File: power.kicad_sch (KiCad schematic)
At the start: 84 parts, among them J5 VJ1, Q1 BC857, Q2 2N7002, U1 LFE5U-85F-6BG381C, U3 TLV62569DBV, U4 TLV62569DBV, U5 TLV62569DBV, U7 MCP7940NT, Y2 32768Hz

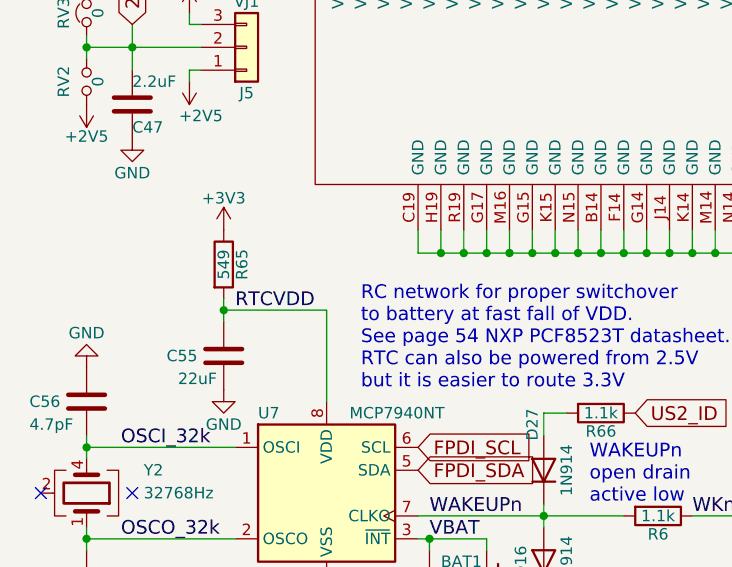
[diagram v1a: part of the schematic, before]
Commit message: add PWR_PIN to RTCVDD
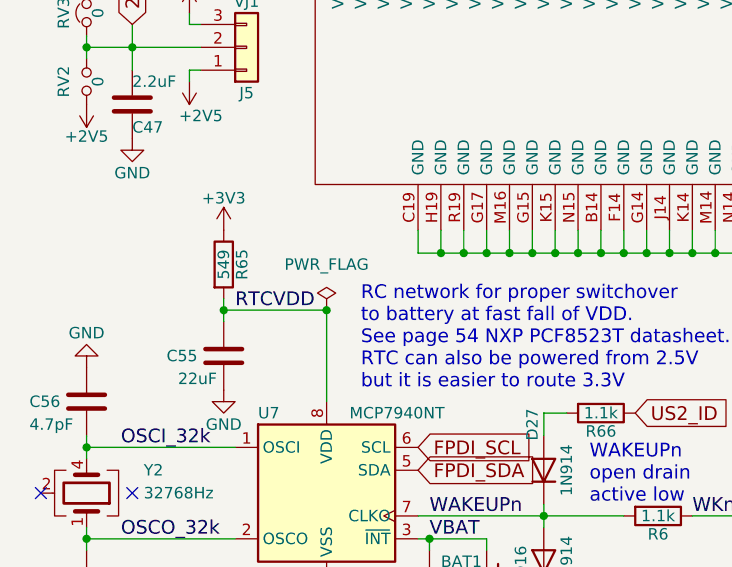
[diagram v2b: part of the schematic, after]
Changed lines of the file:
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@@
 	)
 	(junction
+		(at 49.53 72.39)
+		(diameter 0)
+		(color 0 0 0 0)
+	)
+	(junction
 		(at 247.65 66.04)
 		(diameter 0)
@@
 					(unit 1)
 				)
+			)
+		)
+	)
+	(symbol
+		(lib_id "power:PWR_FLAG")
+		(at 49.53 72.39 0)
+		(unit 1)
+		(exclude_from_sim no)
+		(in_bom yes)
+		(on_board yes)
+		(dnp no)
+		(fields_autoplaced yes)
+		(property "Reference" "#FLG02"
+			(at 49.53 70.485 0)
+			(effects
+				(font
+					(size 1.27 1.27)
+				)
+				(hide yes)
+			)
+		)
+		(property "Value" "PWR_FLAG"
+			(at 49.53 67.31 0)
+			(effects
+				(font
+					(size 1.27 1.27)
+				)
+			)
+		)
+		(property "Footprint" ""
+			(at 49.53 72.39 0)
+			(effects
+				(font
+					(size 1.27 1.27)
+				)
+				(hide yes)
+			)
+		)
+		(property "Datasheet" "~"
+			(at 49.53 72.39 0)
+			(effects
+				(font
+					(size 1.27 1.27)
+				)
+				(hide yes)
+			)
+		)
+		(property "Description" "Special symbol for telling ERC where power comes from"
+			(at 49.53 72.39 0)
+			(effects
+				(font
+					(size 1.27 1.27)
+				)
+				(hide yes)
+			)
+		)
+		(pin "1"
+		)
+		(instances
+			(project "ulx3s"
+				(path "/49a43414-f3c1-43b2-ad20-ac3166075f21/00000000-0000-0000-0000-000058d51cad"
+					(reference "#FLG02")
+					(unit 1)
+				)

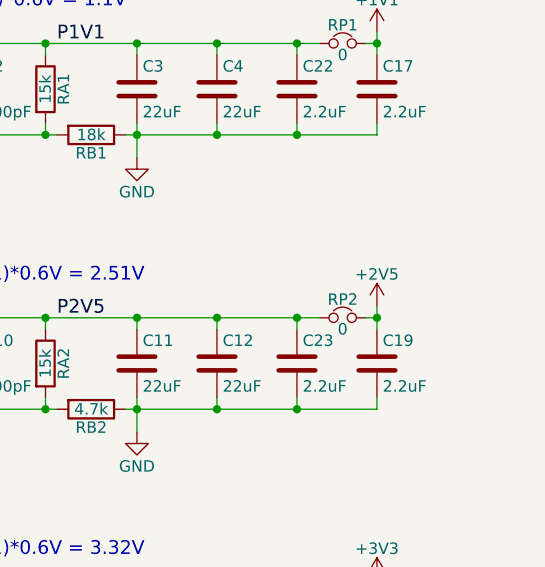
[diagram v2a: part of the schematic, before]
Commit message: add pwr_pin to 2.5v
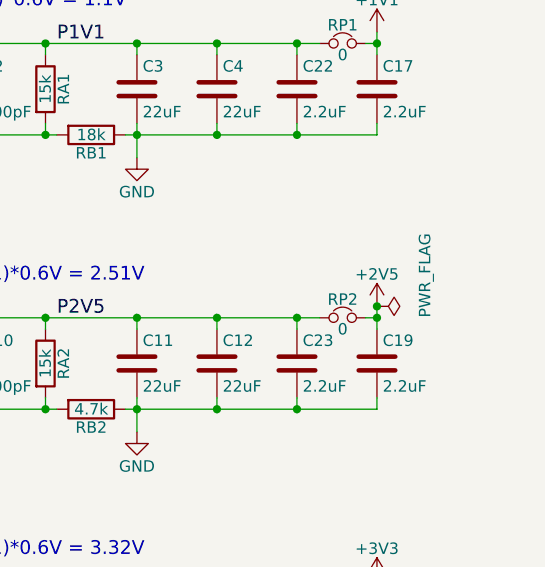
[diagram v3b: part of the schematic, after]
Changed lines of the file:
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@@
 	)
 	(junction
+		(at 275.59 107.95)
+		(diameter 0)
+		(color 0 0 0 0)
+	)
+	(junction
 		(at 104.14 125.73)
 		(diameter 0)
@@
 					(unit 1)
 				)
+			)
+		)
+	)
+	(symbol
+		(lib_id "power:PWR_FLAG")
+		(at 275.59 107.95 270)
+		(unit 1)
+		(exclude_from_sim no)
+		(in_bom yes)
+		(on_board yes)
+		(dnp no)
+		(property "Reference" "#FLG03"
+			(at 277.495 107.95 0)
+			(effects
+				(font
+					(size 1.27 1.27)
+				)
+				(hide yes)
+			)
+		)
+		(property "Value" "PWR_FLAG"
+			(at 280.924 99.822 0)
+			(effects
+				(font
+					(size 1.27 1.27)
+				)
+				(justify left)
+			)
+		)
+		(property "Footprint" ""
+			(at 275.59 107.95 0)
+			(effects
+				(font
+					(size 1.27 1.27)
+				)
+				(hide yes)
+			)
+		)
+		(property "Datasheet" "~"
+			(at 275.59 107.95 0)
+			(effects
+				(font
+					(size 1.27 1.27)
+				)
+				(hide yes)
+			)
+		)
+		(property "Description" "Special symbol for telling ERC where power comes from"
+			(at 275.59 107.95 0)
+			(effects
+				(font
+					(size 1.27 1.27)
+				)
+				(hide yes)
+			)
+		)
+		(pin "1"
+		)
+		(instances
+			(project "ulx3s"
+				(path "/49a43414-f3c1-43b2-ad20-ac3166075f21/00000000-0000-0000-0000-000058d51cad"
+					(reference "#FLG03")
+					(unit 1)
+				)

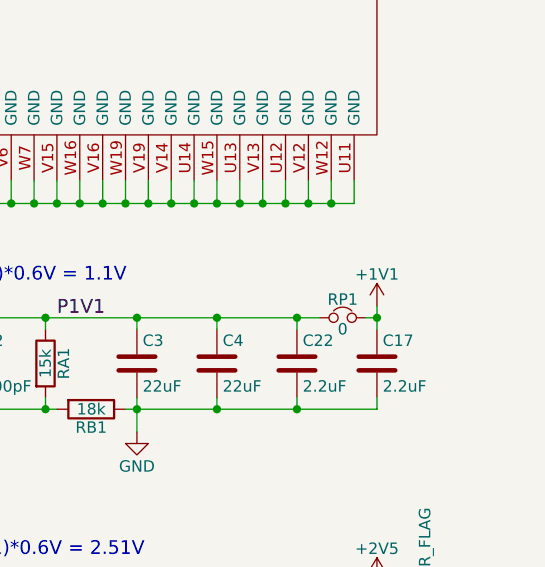
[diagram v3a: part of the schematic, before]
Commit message: add pwr_pin to 1.1v
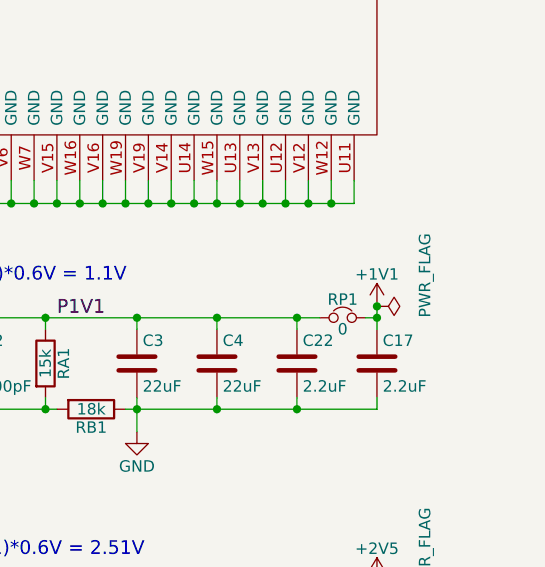
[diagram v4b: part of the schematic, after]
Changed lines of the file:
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@@
 	)
 	(junction
+		(at 275.59 77.47)
+		(diameter 0)
+		(color 0 0 0 0)
+	)
+	(junction
 		(at 93.98 26.67)
 		(diameter 0)
@@
 					(unit 1)
 				)
+			)
+		)
+	)
+	(symbol
+		(lib_id "power:PWR_FLAG")
+		(at 275.59 77.47 270)
+		(unit 1)
+		(exclude_from_sim no)
+		(in_bom yes)
+		(on_board yes)
+		(dnp no)
+		(property "Reference" "#FLG04"
+			(at 277.495 77.47 0)
+			(effects
+				(font
+					(size 1.27 1.27)
+				)
+				(hide yes)
+			)
+		)
+		(property "Value" "PWR_FLAG"
+			(at 280.924 69.342 0)
+			(effects
+				(font
+					(size 1.27 1.27)
+				)
+				(justify left)
+			)
+		)
+		(property "Footprint" ""
+			(at 275.59 77.47 0)
+			(effects
+				(font
+					(size 1.27 1.27)
+				)
+				(hide yes)
+			)
+		)
+		(property "Datasheet" "~"
+			(at 275.59 77.47 0)
+			(effects
+				(font
+					(size 1.27 1.27)
+				)
+				(hide yes)
+			)
+		)
+		(property "Description" "Special symbol for telling ERC where power comes from"
+			(at 275.59 77.47 0)
+			(effects
+				(font
+					(size 1.27 1.27)
+				)
+				(hide yes)
+			)
+		)
+		(pin "1"
+		)
+		(instances
+			(project "ulx3s"
+				(path "/49a43414-f3c1-43b2-ad20-ac3166075f21/00000000-0000-0000-0000-000058d51cad"
+					(reference "#FLG04")
+					(unit 1)
+				)

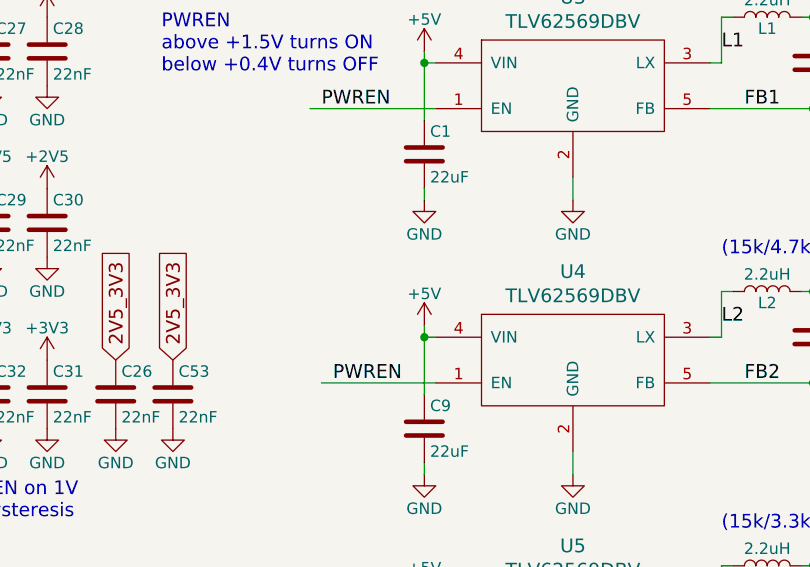
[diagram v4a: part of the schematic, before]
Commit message: add pwr_pin to 5v
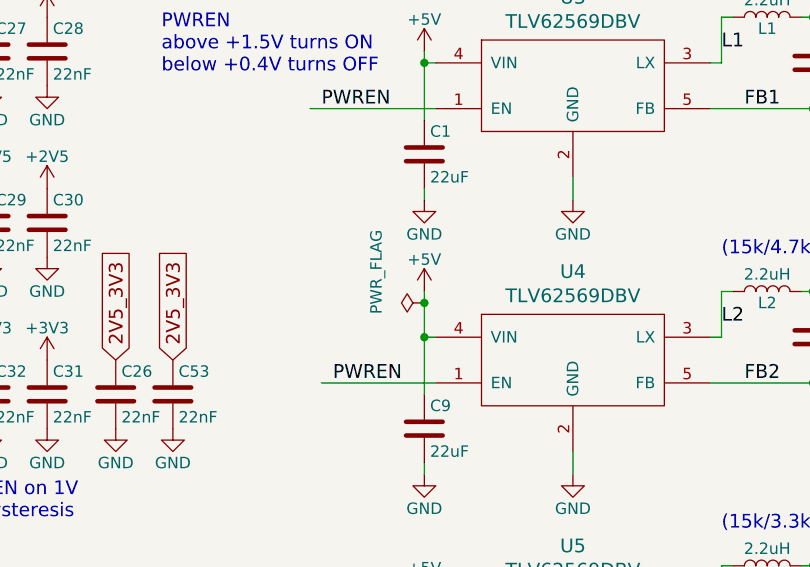
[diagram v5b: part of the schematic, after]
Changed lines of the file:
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@@
 	)
 	(junction
+		(at 187.96 110.49)
+		(diameter 0)
+		(color 0 0 0 0)
+	)
+	(junction
 		(at 222.25 66.04)
 		(diameter 0)
@@
 	(wire
 		(pts
-			(xy 187.96 113.03) (xy 187.96 114.3)
+			(xy 187.96 109.22) (xy 187.96 110.49)
 		)
 		(stroke
@@
 	(wire
 		(pts
+			(xy 187.96 110.49) (xy 187.96 114.3)
+		)
+		(stroke
+			(width 0)
+			(type default)
+		)
+	)
+	(wire
+		(pts
 			(xy 90.17 95.25) (xy 95.25 95.25)
 		)
@@
 	(symbol
 		(lib_id "power:+5V")
-		(at 187.96 113.03 0)
+		(at 187.96 109.22 0)
 		(unit 1)
 		(exclude_from_sim no)
@@
 		(dnp no)
 		(property "Reference" "#PWR067"
-			(at 187.96 116.84 0)
+			(at 187.96 113.03 0)
 			(effects
 				(font
@@
 		)
 		(property "Value" "+5V"
-			(at 187.96 109.474 0)
+			(at 187.96 105.664 0)
 			(effects
 				(font
@@
 		)
 		(property "Footprint" ""
-			(at 187.96 113.03 0)
+			(at 187.96 109.22 0)
 			(effects
 				(font
@@
 		)
 		(property "Datasheet" ""
-			(at 187.96 113.03 0)
+			(at 187.96 109.22 0)
 			(effects
 				(font
@@
 		)
 		(property "Description" ""
-			(at 187.96 113.03 0)
+			(at 187.96 109.22 0)
 			(effects
 				(font
@@
 					(unit 1)
 				)
+			)
+		)
+	)
+	(symbol
+		(lib_id "power:PWR_FLAG")
+		(at 187.96 110.49 90)
+		(mirror x)
+		(unit 1)
+		(exclude_from_sim no)
+		(in_bom yes)
+		(on_board yes)
+		(dnp no)
+		(property "Reference" "#FLG05"
+			(at 186.055 110.49 0)
+			(effects
+				(font
+					(size 1.27 1.27)
+				)
+				(hide yes)
+			)
+		)
+		(property "Value" "PWR_FLAG"
+			(at 182.626 102.362 0)
+			(effects
+				(font
+					(size 1.27 1.27)
+				)
+				(justify left)
+			)
+		)
+		(property "Footprint" ""
+			(at 187.96 110.49 0)
+			(effects
+				(font
+					(size 1.27 1.27)
+				)
+				(hide yes)
+			)
+		)
+		(property "Datasheet" "~"
+			(at 187.96 110.49 0)
+			(effects
+				(font
+					(size 1.27 1.27)
+				)
+				(hide yes)
+			)
+		)
+		(property "Description" "Special symbol for telling ERC where power comes from"
+			(at 187.96 110.49 0)
+			(effects
+				(font
+					(size 1.27 1.27)
+				)
+				(hide yes)
+			)
+		)
+		(pin "1"
+		)
+		(instances
+			(project "ulx3s"
+				(path "/49a43414-f3c1-43b2-ad20-ac3166075f21/00000000-0000-0000-0000-000058d51cad"
+					(reference "#FLG05")
+					(unit 1)
+				)

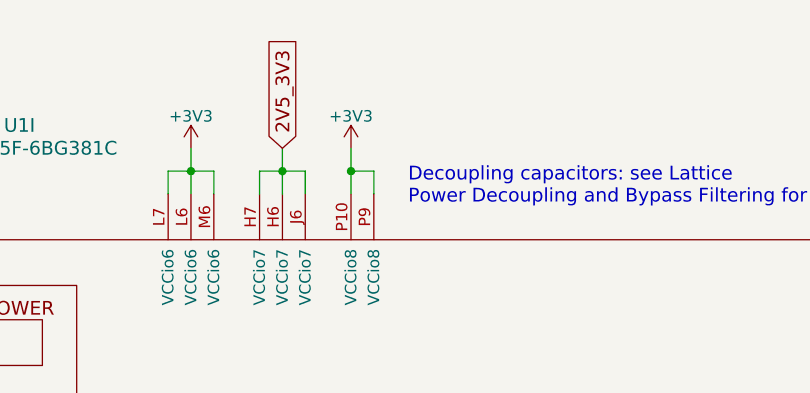
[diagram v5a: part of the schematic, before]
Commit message: add pwr_flag to +3V3
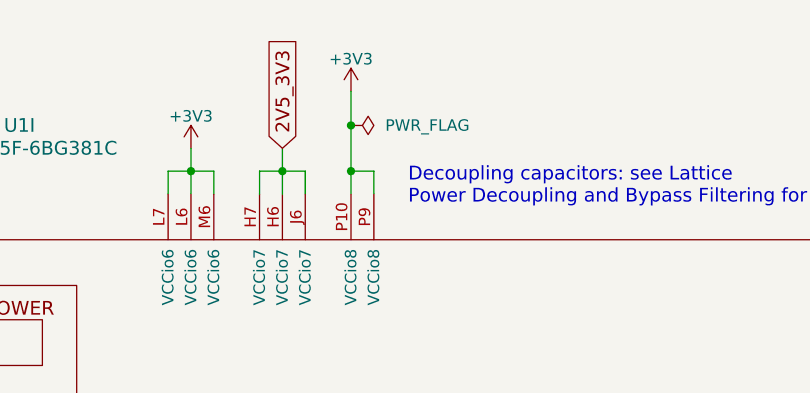
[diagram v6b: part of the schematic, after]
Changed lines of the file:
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@@
 	)
 	(junction
+		(at 194.31 21.59)
+		(diameter 0)
+		(color 0 0 0 0)
+	)
+	(junction
 		(at 64.77 66.04)
 		(diameter 0)
@@
 	(wire
 		(pts
-			(xy 194.31 24.13) (xy 194.31 26.67)
+			(xy 194.31 17.78) (xy 194.31 21.59)
 		)
 		(stroke
@@
 	(wire
 		(pts
+			(xy 194.31 21.59) (xy 194.31 26.67)
+		)
+		(stroke
+			(width 0)
+			(type default)
+		)
+	)
+	(wire
+		(pts
 			(xy 191.77 63.5) (xy 191.77 66.04)
 		)
@@
 	(symbol
 		(lib_id "power:+3V3")
-		(at 194.31 24.13 0)
+		(at 194.31 17.78 0)
 		(unit 1)
 		(exclude_from_sim no)
@@
 		(dnp no)
 		(property "Reference" "#PWR071"
-			(at 194.31 27.94 0)
+			(at 194.31 21.59 0)
 			(effects
 				(font
@@
 		)
 		(property "Value" "+3V3"
-			(at 194.31 20.574 0)
+			(at 194.31 14.224 0)
 			(effects
 				(font
@@
 		)
 		(property "Footprint" ""
-			(at 194.31 24.13 0)
+			(at 194.31 17.78 0)
 			(effects
 				(font
@@
 		)
 		(property "Datasheet" ""
-			(at 194.31 24.13 0)
+			(at 194.31 17.78 0)
 			(effects
 				(font
@@
 		)
 		(property "Description" ""
-			(at 194.31 24.13 0)
+			(at 194.31 17.78 0)
 			(effects
 				(font
@@
 					(unit 1)
 				)
+			)
+		)
+	)
+	(symbol
+		(lib_id "power:PWR_FLAG")
+		(at 194.31 21.59 270)
+		(unit 1)
+		(exclude_from_sim no)
+		(in_bom yes)
+		(on_board yes)
+		(dnp no)
+		(fields_autoplaced yes)
+		(property "Reference" "#FLG08"
+			(at 196.215 21.59 0)
+			(effects
+				(font
+					(size 1.27 1.27)
+				)
+				(hide yes)
+			)
+		)
+		(property "Value" "PWR_FLAG"
+			(at 198.12 21.5899 90)
+			(effects
+				(font
+					(size 1.27 1.27)
+				)
+				(justify left)
+			)
+		)
+		(property "Footprint" ""
+			(at 194.31 21.59 0)
+			(effects
+				(font
+					(size 1.27 1.27)
+				)
+				(hide yes)
+			)
+		)
+		(property "Datasheet" "~"
+			(at 194.31 21.59 0)
+			(effects
+				(font
+					(size 1.27 1.27)
+				)
+				(hide yes)
+			)
+		)
+		(property "Description" "Special symbol for telling ERC where power comes from"
+			(at 194.31 21.59 0)
+			(effects
+				(font
+					(size 1.27 1.27)
+				)
+				(hide yes)
+			)
+		)
+		(pin "1"
+		)
+		(instances
+			(project "ulx3s"
+				(path "/49a43414-f3c1-43b2-ad20-ac3166075f21/00000000-0000-0000-0000-000058d51cad"
+					(reference "#FLG08")
+					(unit 1)
+				)

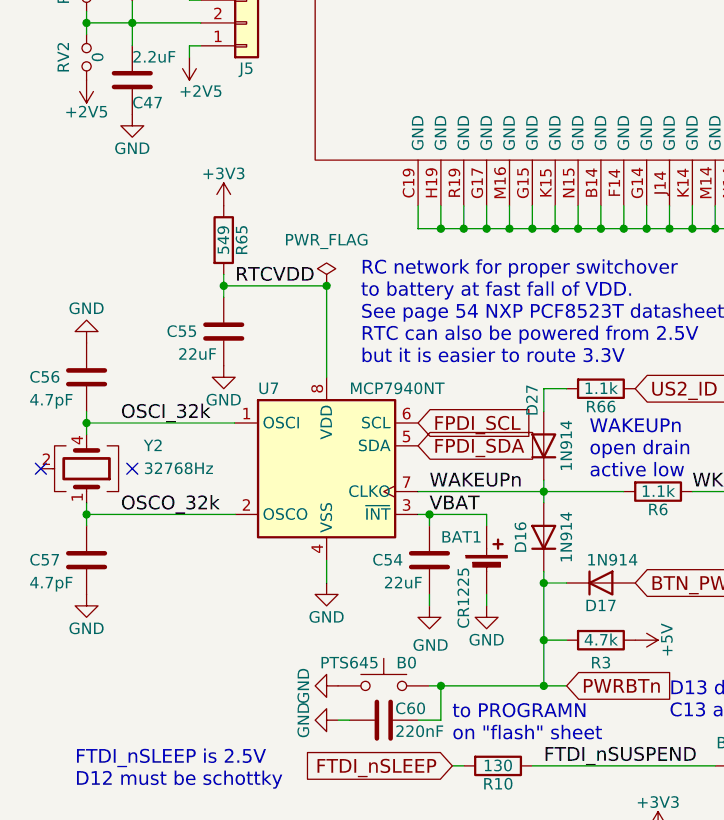
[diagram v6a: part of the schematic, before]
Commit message: remove unneeded components from schema
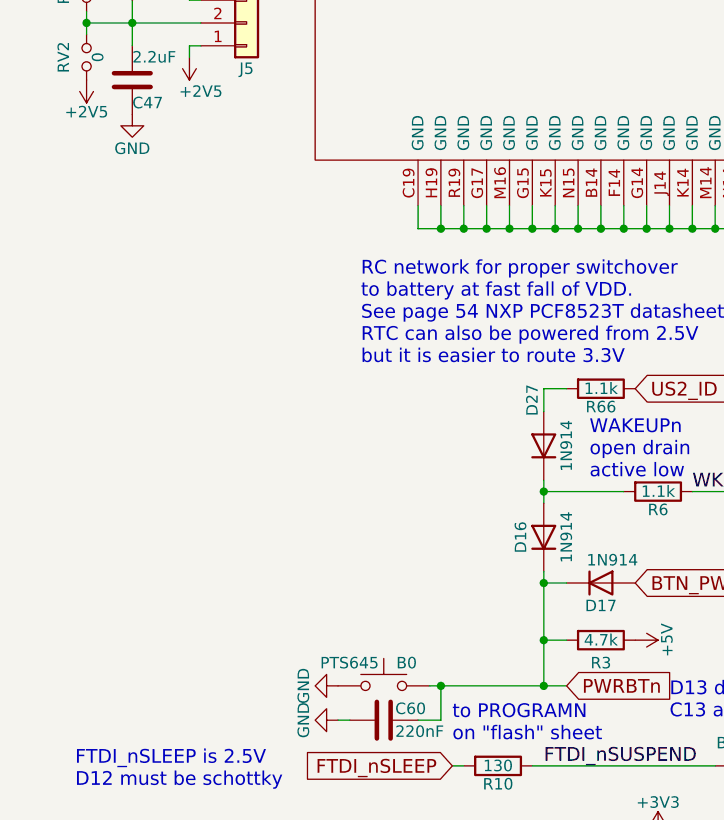
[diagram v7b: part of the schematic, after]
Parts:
- removed BAT1: CR1225, Keystone_3000_1x12mm-CoinCell:Keystone_3000_1x12mm-CoinCell, symbol Device:Battery_Cell
- removed C54, C55: 22uF, Capacitor_SMD:C_0805_2012Metric, symbol Device:C
- removed C56, C57: 4.7pF, Capacitor_SMD:C_0603_1608Metric, symbol Device:C
- removed R65: 549, Resistor_SMD:R_0603_1608Metric, symbol Device:R
- removed U7: MCP7940NT, SOT96-1:SOT96-1, symbol Timer_RTC:PCF8563T
- removed Y2: 32768Hz, abs07:Crystal_SMD_ABS07, symbol Device:Crystal_GND23
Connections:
- net WAKEUPn: no longer names the net of D16.2 (A), D27.1 (K), R6.2
- no-connect marks 2 -> 0

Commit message: start to normalize bom
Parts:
- C10, C6: Digikey (none) -> 311-4078-1-ND; LCSC (none) -> C14665; LCS_C2 (none) -> C22396; MPN (none) -> CS0603KRX7R9BB471
- C11, C12, C3, C4, C7, C8: Digikey (none) -> 1276-2413-1-ND; LCSC (none) -> C29277; MPN (none) -> CC0805ZKY5V5BB226
- C17, C19, C20, C22, C23, C24: Digikey (none) -> 587-5918-1-ND; LCSC (none) -> C87995; MPN (none) -> CC0805MRX5R6BB225
- C26, C27, C28, C29, C30, C31, C32, C48, C49, C50, C51, C53: Digikey (none) -> 587-1238-1-ND; LCSC (none) -> C107137
- C47: Digikey (none) -> 587-5918-1-ND; LCSC (none) -> C87995
- C5, C9: Digikey (none) -> 1276-2413-1-ND; LCSC (none) -> C29277
- C60: Digikey (none) -> 1276-1112-1-ND; LCSC (none) -> C326805; MPN (none) -> CC0603KRX7R8BB224
- D10, D13, D14, D17, D27: Chip1stop (none) -> C1S541901230010; Digikey (none) -> 1N914BWSCT-ND; LCSC (none) -> C258181; MPN (none) -> 1N4148WS
- D11: Digikey (none) -> 160-1415-1-ND; LCSC (none) -> C94868; MPN (none) -> LTST-C170KRKT
- D12: Digikey (none) -> NSR0530HT1GOSCT-ND; LCSC (none) -> C12744; MPN (none) -> NSR0530HT1G
- J5, RP1, RP2, RP3, RV2, RV3: now left out of the parts list
- L2, L3: Digikey (none) -> 445-TFM322512ALMA2R2MTAACT-ND; LCSC (none) -> C285758; LCS_C2 (none) -> C285914; MPN (none) -> DFE322512F-2R2M=P2
- R13, RA2, RA3: Digikey (none) -> YAG3569CT-ND; LCSC (none) -> C217750; MPN (none) -> RC0603FR-0715KL
- R2: Digikey (none) -> 311-18.0KHRCT-ND; LCSC (none) -> C425614; MPN (none) -> RC0603FR-1018KL
- R3, R4, RB2: Digikey (none) -> YAG3613CT-ND; LCSC (none) -> C218056
- RA1: Digikey (none) -> YAG3569CT-ND; LCSC (none) -> C217750; MPN RC0603FR-1015KL -> RC0603FR-0715KL
- U1: Digikey (none) -> 220-2177-ND; LCSC (none) -> C446029
- U4, U5: Digikey (none) -> 296-47360-1-ND; LCSC (none) -> C141836
